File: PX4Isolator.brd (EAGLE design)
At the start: 49.1 x 15.3 mm, 22 parts, among them J1 DF13C-6P-1.25V, J2 DF13-4P-1.25V, J201 DF13C-6P-1.25V, J403 DF13C-7P-1.25V

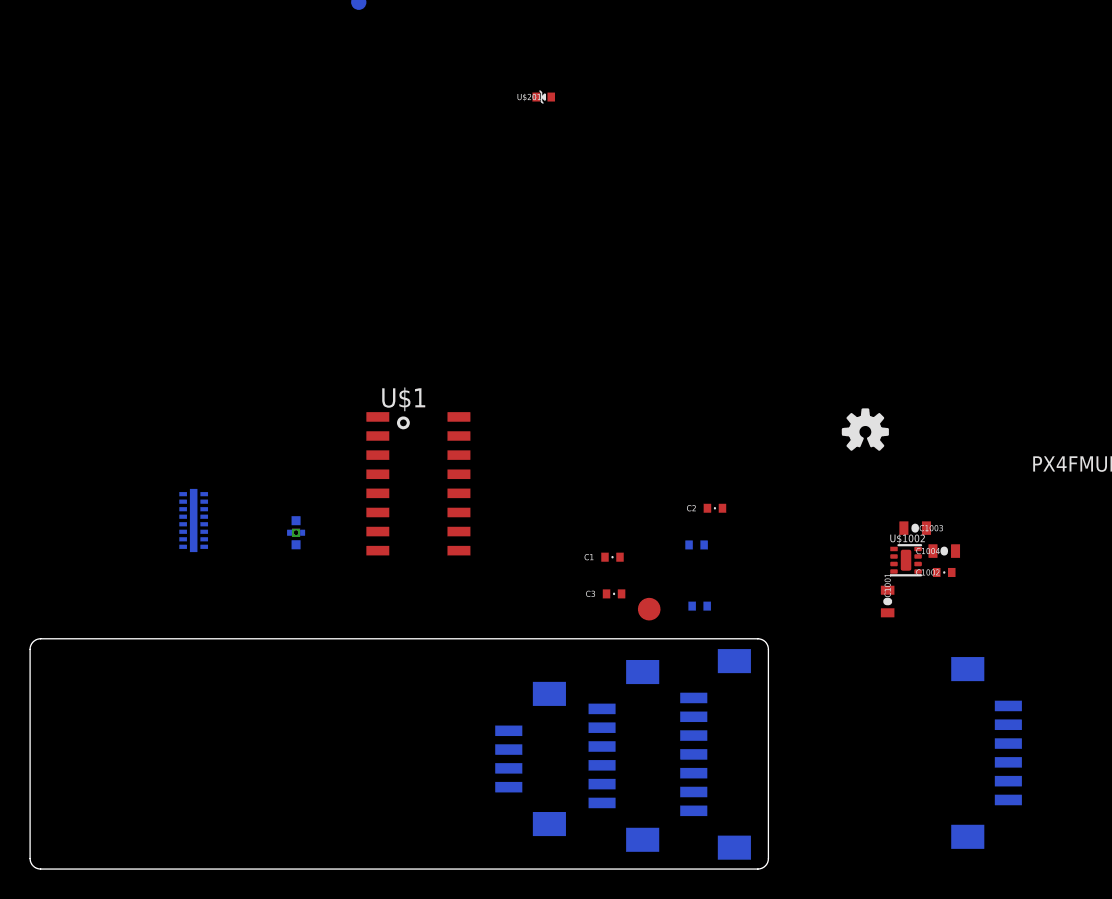
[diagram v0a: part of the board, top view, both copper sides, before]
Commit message: Isolator peripheral side signals done
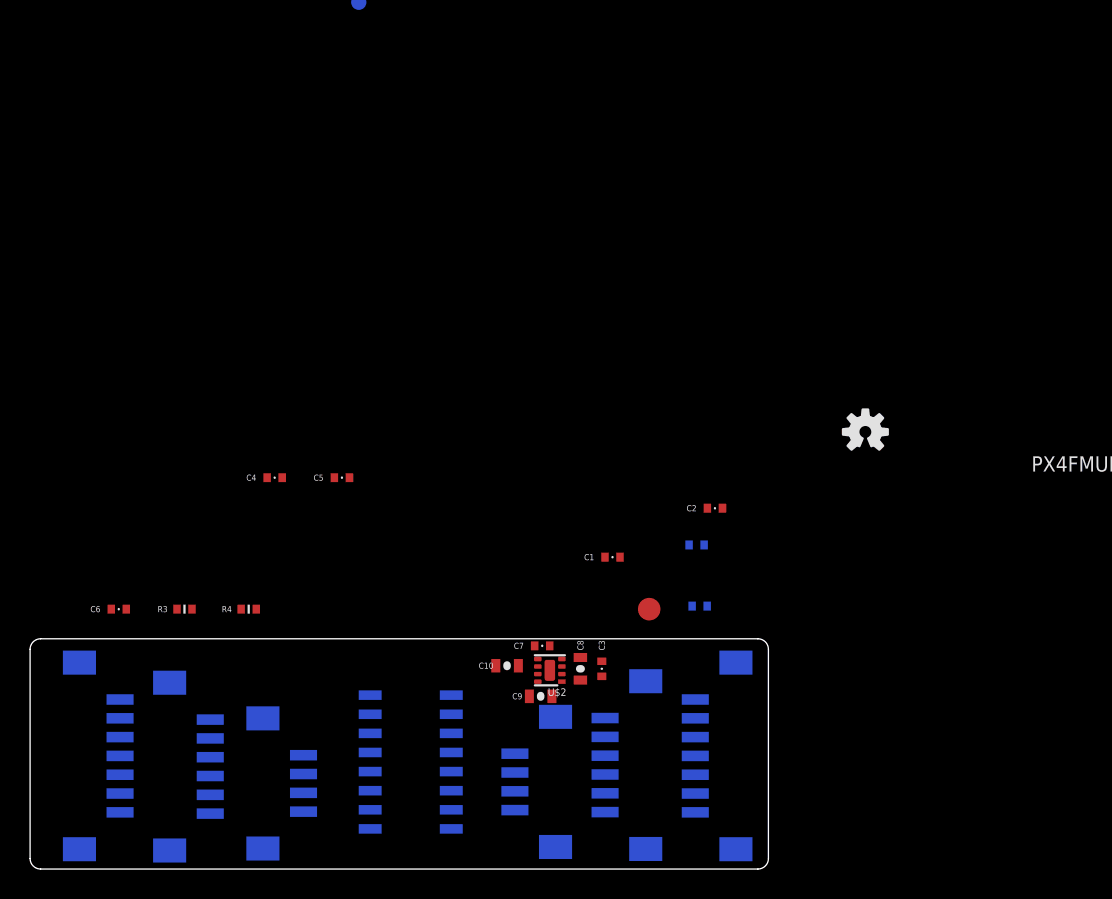
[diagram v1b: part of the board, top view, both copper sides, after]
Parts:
- removed C1001, C1003, C1004: 1u0, pixhawk2:0603-CAP
- removed C1002: 10n, pixhawk2:0402-CAP
- removed J201: DF13C-6P-1.25V, con-hirose-df13:DF13C-6P-1.25V
- removed J403: DF13C-7P-1.25V, con-hirose-df13:DF13C-7P-1.25V
- removed L2: NUF8402MN, PX4lite:DFN16-THIN
- removed L201: KNH16C104DA5TS, pixhawk2:KYOCERA-KNH16-DA
- removed U$1002: MIC5332, pixhawk2:MLF-8-EPAD
- removed U$201: PESD0402-140, pixhawk2:0402-TVS
- added C10, C8, C9: 1u0, pixhawk2:0603-CAP
- added C4, C5, C6: 0u1, pixhawk2:0402-CAP
- added C7: 10n, pixhawk2:0402-CAP
- added J3, J6: DF13C-7P-1.25V, con-hirose-df13:DF13C-7P-1.25V
- added J4: DF13-4P-1.25V, con-hirose-df13:DF13C-4P-1.25V
- added J5: DF13C-6P-1.25V, con-hirose-df13:DF13C-6P-1.25V
- added R3, R4: 1K5, pixhawk2:0402-RES
- added U$2: MIC5332, pixhawk2:MLF-8-EPAD
- moved U$1 18.5 mm to (34.5, 9.86), flipped to the bottom
- moved C3 5.04 mm to (47.2, 16.1), turned to 270 degrees
- moved J2 1.58 mm to (42.4, 8.53)
- moved J1 0.64 mm to (48.4, 9.65)
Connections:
- net VCCB renamed VDD_3V3_ISOL
- removed net !SPI_EXT_NSS: J403.P$5
- removed net FMU-I2C_SCL: J2.P$2, R1.P$1
- removed net FMU-I2C_SDA: J2.P$3, R2.P$1
- removed net FMU-USART2_CTS: L2.P$8
- removed net FMU-USART2_RTS: L2.P$7
- removed net FMU-USART2_RX: L2.P$5
- removed net FMU-USART2_TX: L2.P$6
- removed net FMU-USART3_CTS: L2.P$2
- removed net FMU-USART3_RTS: L2.P$1
- removed net FMU-USART3_RX: L2.P$3
- removed net FMU-USART3_TX: L2.P$4
- removed net FMU-VDD_5V: C1001.P$1, U$1002.1, U$1002.4, U$1002.5
- removed net GNDA: U$1.8
- removed net GNDB: U$1.9
- removed net GNDX: C1.P$2, C1001.P$2, C1002.P$2, C1003.P$2, C1004.P$2, C3.P$2, GND..P$1, J1.P$6, J201.P$6, J403.P$7, L201.P$3, L201.P$4, L201.P$5, U$1002.2, U$1002.GND, U$201.A
- removed net GPIO_EXT_1: J403.P$6
- removed net N$104: C1002.P$1, U$1002.6
- removed net N$5: J201.P$1, L201.P$2, U$201.C
- removed net SERIAL1_CTS: J201.P$4, L2.P$9
- removed net SERIAL1_RTS: J201.P$5, L2.P$10
- removed net SERIAL1_RX: J201.P$3, L2.P$12
- removed net SERIAL1_TX: J201.P$2, L2.P$11
- removed net SERIAL2_CTS: J1.P$4, L2.P$15
- removed net SERIAL2_RTS: J1.P$5, L2.P$16
- removed net SERIAL2_RX: J1.P$3, L2.P$14
- removed net SERIAL2_TX: J1.P$2, L2.P$13
- removed net SPI_EXT_MISO: J403.P$3
- removed net SPI_EXT_MOSI: J403.P$4
- removed net SPI_EXT_SCK: J403.P$2
- removed net VCCA: U$1.1
- removed net VDD_3V3_PERIPH: C1004.P$1, U$1002.7
- removed net VDD_5V_HIPOWER: L201.P$1
- removed net VDD_5V_PERIPH: C1.P$1, C2.P$1, C3.P$1, J1.P$1, J2.P$1, J403.P$1
- new net GND_ISOL: C4.P$2, C5.P$2, C6.P$2, J4.P$4, J5.P$6, J6.P$7, U$1.9
- new net MASTER_IN1: J1.P$3, J3.P$3, U$1.2
- new net MASTER_IN2: U$1.3
- new net MASTER_IO1: J1.P$4, J2.P$2, J3.P$5, R1.P$1, U$1.6
- new net MASTER_IO2: J1.P$5, J2.P$3, J3.P$6, R2.P$1, U$1.7
- new net MASTER_OUT1: J1.P$2, J3.P$4, U$1.4
- new net MASTER_OUT2: J3.P$2, U$1.5
- new net N$1: C7.P$1, U$2.6
- new net PERIPH_IN1: J5.P$3, J6.P$3, U$1.13
- new net PERIPH_IN2: U$1.12
- new net PERIPH_IO1: J4.P$2, J5.P$4, J6.P$5, R3.P$1, U$1.15
- new net PERIPH_IO2: J4.P$3, J5.P$5, J6.P$6, R4.P$1, U$1.14
- new net PERIPH_OUT1: J5.P$2, J6.P$4, U$1.11
- new net PERIPH_OUT2: J6.P$2, U$1.10
- new net VDD_3V3_MASTER: C10.P$1, U$2.7
- new net VDD_5V_MASTER: C1.P$1, C2.P$1, C3.P$1, C4.P$1, C5.P$1, C6.P$1, C8.P$1, J1.P$1, J2.P$1, J3.P$1, J4.P$1, J5.P$1, J6.P$1, U$2.1, U$2.4, U$2.5
- net GND: now also C1.P$2, C10.P$2, C3.P$2, C7.P$2, C8.P$2, C9.P$2, GND..P$1, J1.P$6, J3.P$7, U$1.8, U$2.2, U$2.GND; no longer L2.P$EP
- net VDD_3V3: now also C9.P$1, R3.P$2, R4.P$2, U$1.1, U$2.8; no longer C1003.P$1, U$1002.8
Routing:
- added copper zone on layer 2, net GND
- removed copper zone on layer 2, net GNDX
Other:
- board text added: "UART"
- board text removed: "AUX ADC"
- board text removed: "SER2"

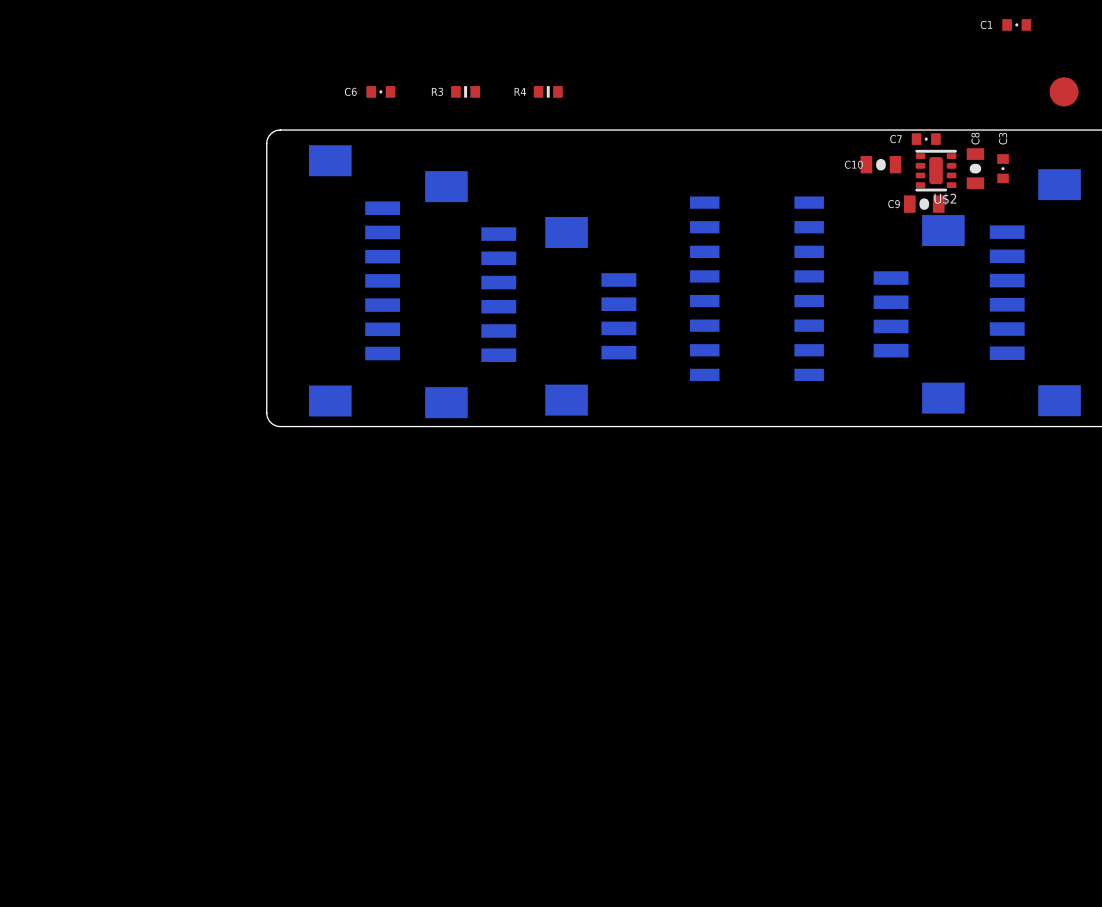
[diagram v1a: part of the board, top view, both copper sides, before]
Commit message: Regulator added
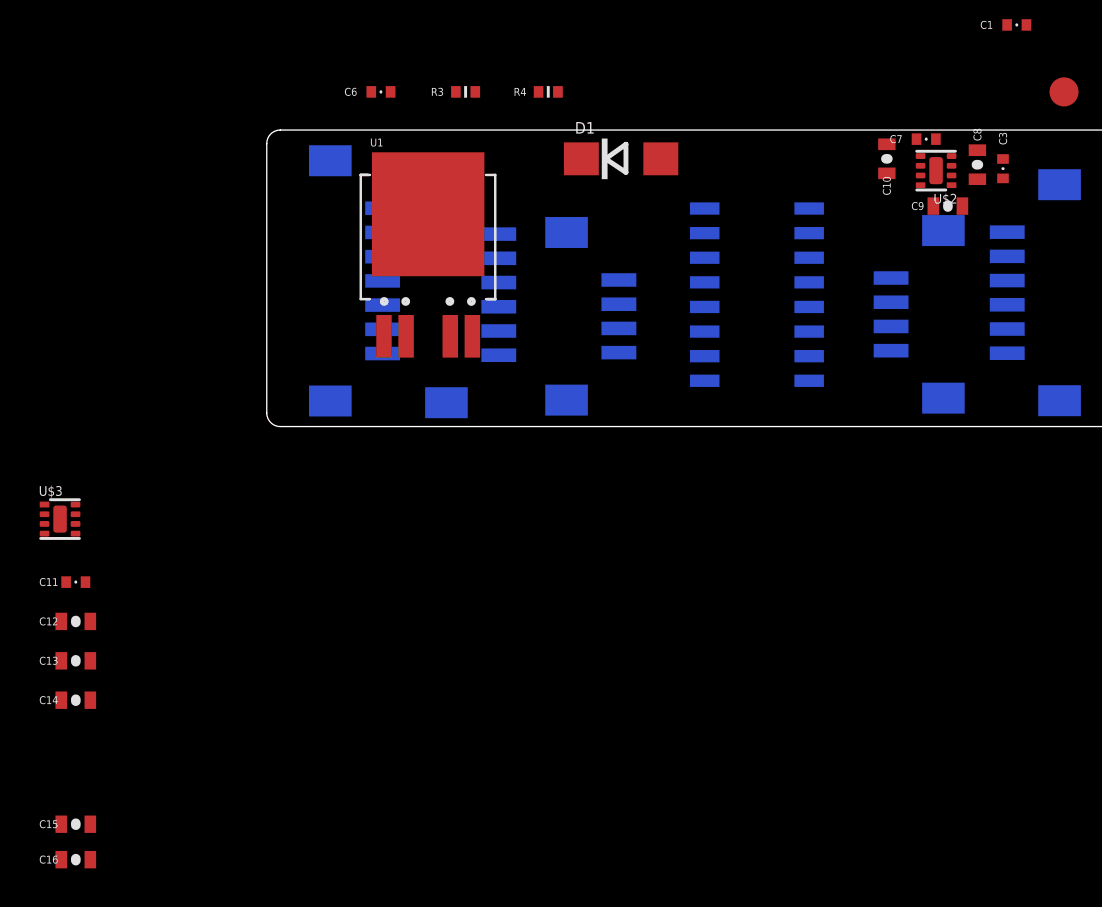
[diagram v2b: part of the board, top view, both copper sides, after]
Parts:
- added C11: 10n, pixhawk2:0402-CAP
- added C12, C13, C14: 1u0, pixhawk2:0603-CAP
- added C15, C16: (no value), PX4FMUlite_V0_1:0603-CAP
- added D1: DIODE-SCHOTTKY_DO214, PX4FMUlite_V0_1:DO214AC
- added U$3: MIC5332, pixhawk2:MLF-8-EPAD
- added U1: V_REG_NCP50X, SparkFun-PowerIC:DPAK-5
- moved C9 1.22 mm to (44.4, 14.1)
- moved C10 0.43 mm to (41.2, 16.6), turned to 90 degrees
- moved U$1 0.30 mm to (34.5, 9.55)
- moved C8 0.23 mm to (45.9, 16.3)
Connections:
- new net N$2: C11.P$1, U$3.6
- new net N$3: C15.P$1, D1.C, U1.EN, U1.VIN
- new net VDD_3V3_ISOL2: C14.P$1, U$3.7
- new net VDD_5V_ISOL: C12.P$1, C16.P$1, C4.P$1, C5.P$1, C6.P$1, J4.P$1, J5.P$1, J6.P$1, U$3.1, U$3.4, U$3.5, U1.VOUT
- new net VIN_ISOL: D1.A
- net GND: now also C11.P$2, C12.P$2, C13.P$2, C14.P$2, U$3.2, U$3.GND
- net GND_ISOL: now also C15.P$2, C16.P$2, U1.GND
- net VDD_3V3_ISOL: now also C13.P$1, U$3.8
- net VDD_5V_MASTER: no longer C4.P$1, C5.P$1, C6.P$1, J4.P$1, J5.P$1, J6.P$1

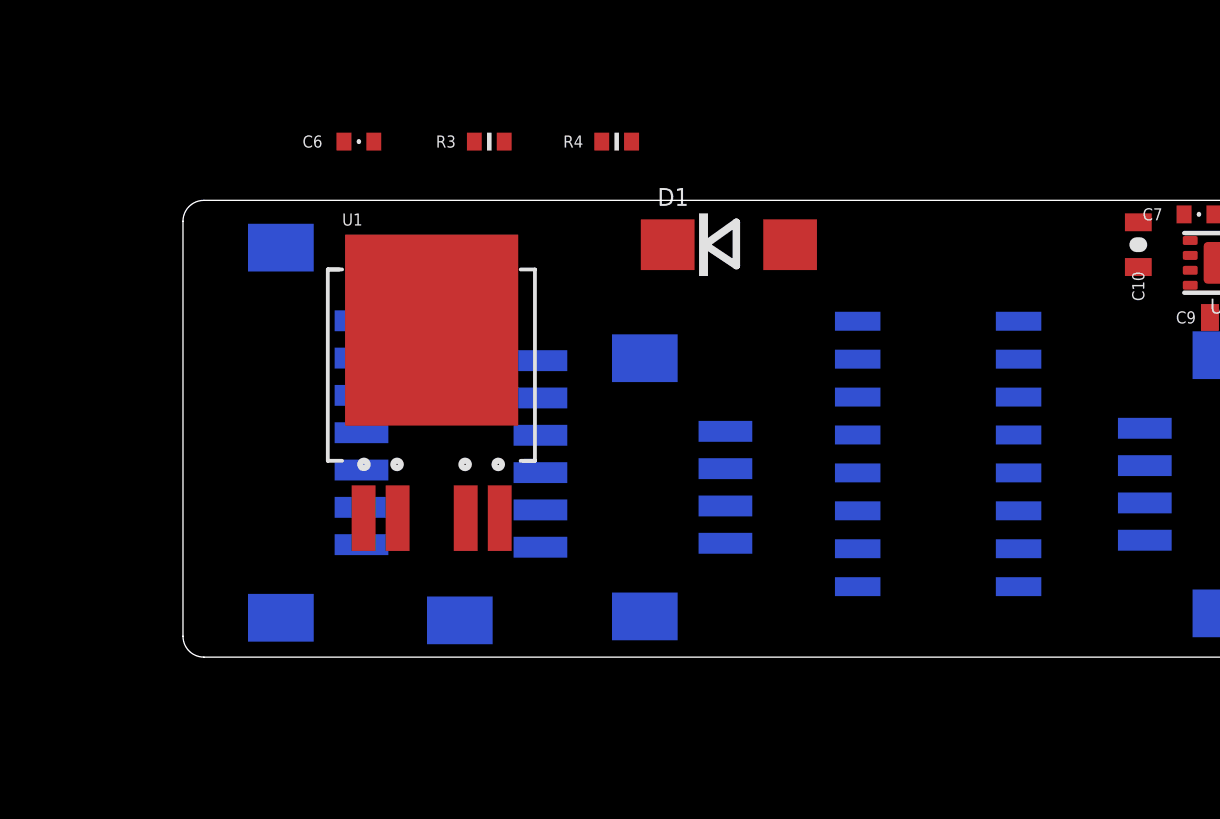
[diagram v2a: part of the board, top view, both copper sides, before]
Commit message: Added TPS62143 buck, moved mounting points
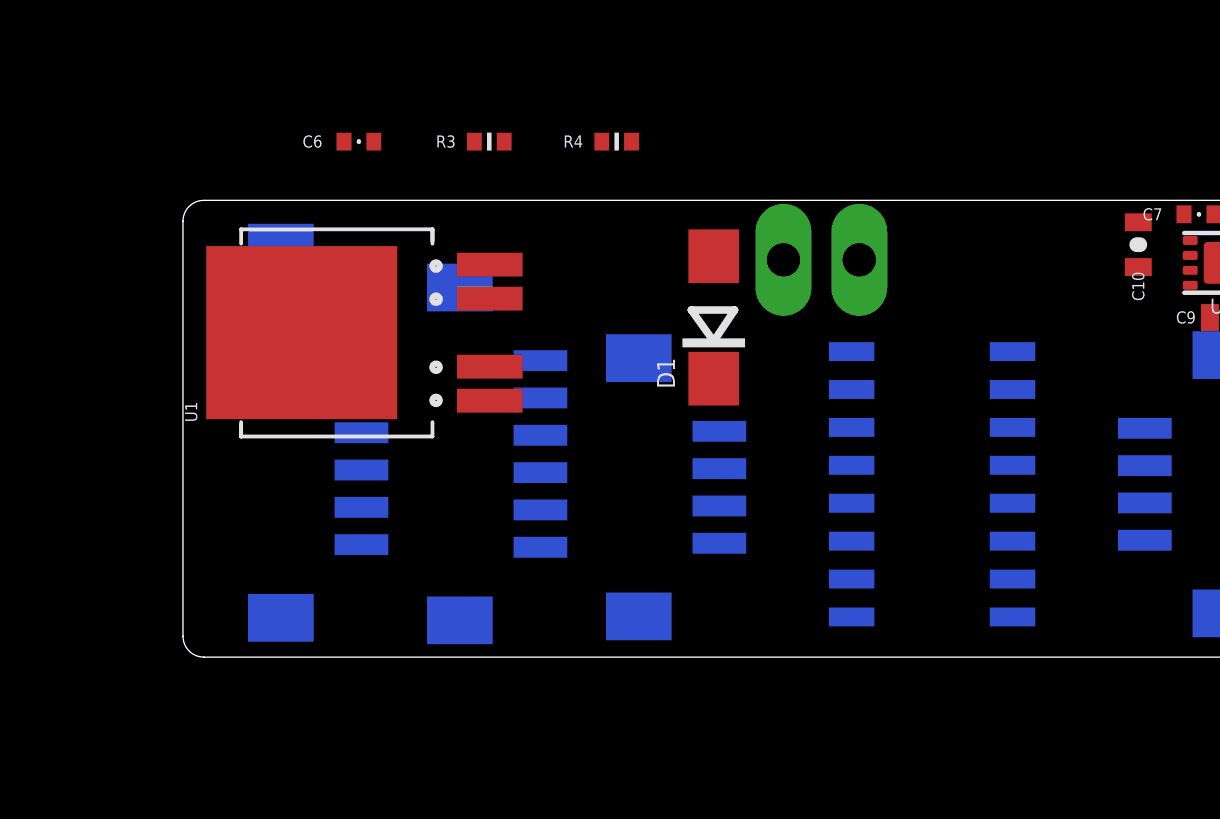
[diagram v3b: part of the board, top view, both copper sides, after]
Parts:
- added JP3: M02PTH3, SparkFun-Connectors:1X02_LONGPADS
- moved U1 3.48 mm to (14.2, 13.6), turned to 90 degrees
- moved D1 2.49 mm to (27.0, 14.1), turned to 90 degrees
- moved U$1 1.04 mm to (34.3, 8.53)
- moved J4 0.20 mm to (26.3, 8.43)
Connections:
- net GND_ISOL: now also JP3.1
- net VIN_ISOL: now also JP3.2
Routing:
- removed copper zone on layer 2, net GND
- removed copper zone on layer 14, net VDD_SERVO
